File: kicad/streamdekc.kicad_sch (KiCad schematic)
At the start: 26 parts, among them IC1 74HC4051P, IC2 74HC4051P, SW1 SW_DIP_x01, SW2 SW_DIP_x01, SW3 SW_DIP_x01, SW4 SW_DIP_x01, SW5 SW_DIP_x01, SW6 SW_DIP_x01, SW7 SW_DIP_x01, SW8 SW_DIP_x01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

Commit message: Initial pcb design
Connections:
- net SW1: now also SW1.1
- net SW2: now also SW2.1
- net SW3: now also SW3.1
- net SW4: now also SW4.1
- net SW5: now also SW5.1
- net SW6: now also SW6.1
- net SW7: now also SW7.1
- net SW8: now also SW8.1
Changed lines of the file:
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@@
+    (stroke (width 0) (type default) (color 0 0 0 0))
+  )
+  (wire (pts (xy 87.63 73.66) (xy 90.17 73.66))
     (stroke (width 0) (type default) (color 0 0 0 0))
   )
@@
     (stroke (width 0) (type default) (color 0 0 0 0))
   )
+  (wire (pts (xy 87.63 62.23) (xy 90.17 62.23))
+    (stroke (width 0) (type default) (color 0 0 0 0))
+  )
   (wire (pts (xy 29.21 95.25) (xy 34.29 95.25))
     (stroke (width 0) (type default) (color 0 0 0 0))
@@
     (stroke (width 0) (type default) (color 0 0 0 0))
   )
+  (wire (pts (xy 114.3 73.66) (xy 116.84 73.66))
+    (stroke (width 0) (type default) (color 0 0 0 0))
+  )
   (wire (pts (xy 80.01 128.27) (xy 87.63 128.27))
     (stroke (width 0) (type default) (color 0 0 0 0))
@@
     (stroke (width 0) (type default) (color 0 0 0 0))
   )
+  (wire (pts (xy 87.63 96.52) (xy 90.17 96.52))
+    (stroke (width 0) (type default) (color 0 0 0 0))
+  )
   (wire (pts (xy 80.01 115.57) (xy 87.63 115.57))
     (stroke (width 0) (type default) (color 0 0 0 0))
@@
     (stroke (width 0) (type default) (color 0 0 0 0))
   )
+  (wire (pts (xy 114.3 62.23) (xy 116.84 62.23))
+    (stroke (width 0) (type default) (color 0 0 0 0))
+  )
   (wire (pts (xy 95.25 35.56) (xy 95.25 30.48))
     (stroke (width 0) (type default) (color 0 0 0 0))
@@
     (stroke (width 0) (type default) (color 0 0 0 0))
   )
+  (wire (pts (xy 87.63 85.09) (xy 90.17 85.09))
+    (stroke (width 0) (type default) (color 0 0 0 0))
+  )
   (wire (pts (xy 179.07 95.25) (xy 179.07 100.33))
     (stroke (width 0) (type default) (color 0 0 0 0))
@@
     (stroke (width 0) (type default) (color 0 0 0 0))
   )
+  (wire (pts (xy 114.3 85.09) (xy 116.84 85.09))
+    (stroke (width 0) (type default) (color 0 0 0 0))
+  )
   (wire (pts (xy 180.34 36.83) (xy 184.15 36.83))
     (stroke (width 0) (type default) (color 0 0 0 0))
@@
     (stroke (width 0) (type default) (color 0 0 0 0))
   )
+  (wire (pts (xy 114.3 96.52) (xy 116.84 96.52))
+    (stroke (width 0) (type default) (color 0 0 0 0))
+  )
   (wire (pts (xy 41.91 120.65) (xy 49.53 120.65))
     (stroke (width 0) (type default) (color 0 0 0 0))
@@
     (effects (font (size 1.27 1.27)) (justify left bottom))
   )
+  (label "SW2" (at 87.63 73.66 0)
+    (effects (font (size 1.27 1.27)) (justify left bottom))
+  )
   (label "D9" (at 49.53 39.37 0)
     (effects (font (size 1.27 1.27)) (justify left bottom))
   )
+  (label "SW1" (at 87.63 62.23 0)
+    (effects (font (size 1.27 1.27)) (justify left bottom))
+  )
   (label "3V3" (at 46.99 82.55 0)
     (effects (font (size 1.27 1.27)) (justify left bottom))
@@
     (effects (font (size 1.27 1.27)) (justify left bottom))
   )
+  (label "SW8" (at 114.3 96.52 0)
+    (effects (font (size 1.27 1.27)) (justify left bottom))
+  )
   (label "SDA_5V" (at 80.01 118.11 0)
     (effects (font (size 1.27 1.27)) (justify left bottom))
@@
     (effects (font (size 1.27 1.27)) (justify left bottom))
   )
+  (label "SW4" (at 87.63 96.52 0)
+    (effects (font (size 1.27 1.27)) (justify left bottom))
+  )
+  (label "SW6" (at 114.3 73.66 0)
+    (effects (font (size 1.27 1.27)) (justify left bottom))
+  )
   (label "SCL_5V" (at 184.15 77.47 0)
     (effects (font (size 1.27 1.27)) (justify left bottom))
@@
     (effects (font (size 1.27 1.27)) (justify left bottom))
   )
+  (label "SW7" (at 114.3 85.09 0)
+    (effects (font (size 1.27 1.27)) (justify left bottom))
+  )
   (label "SCL_5V" (at 160.02 97.79 0)
     (effects (font (size 1.27 1.27)) (justify left bottom))
@@
     (effects (font (size 1.27 1.27)) (justify left bottom))
   )
+  (label "SW5" (at 114.3 62.23 0)
+    (effects (font (size 1.27 1.27)) (justify left bottom))
+  )
   (label "DISP_5_SDA" (at 24.13 55.88 0)
     (effects (font (size 1.27 1.27)) (justify left bottom))
@@
     (effects (font (size 1.27 1.27)) (justify left bottom))
   )
+  (label "SW3" (at 87.63 85.09 0)
+    (effects (font (size 1.27 1.27)) (justify left bottom))
+  )

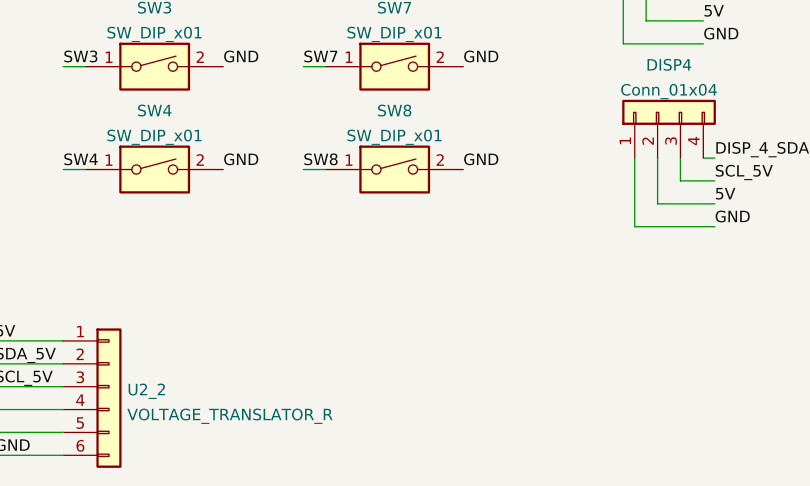
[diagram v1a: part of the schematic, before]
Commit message: Update assembly instructions on B.Silkscreen
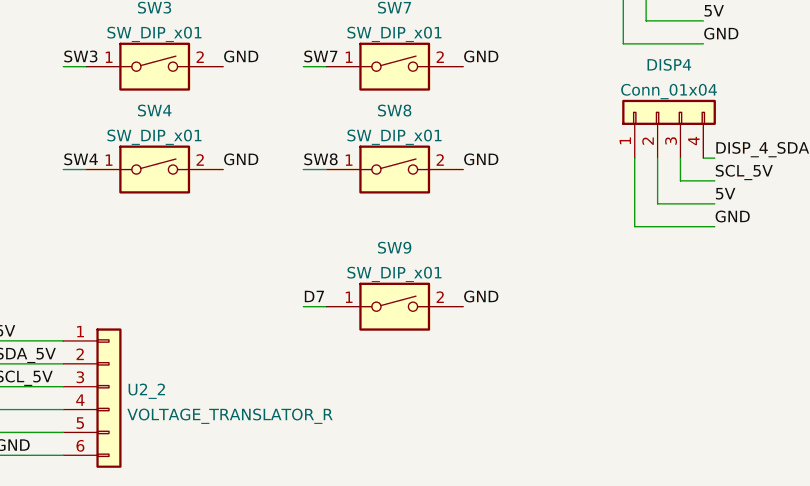
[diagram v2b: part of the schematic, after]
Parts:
- added SW9: SW_DIP_x01, Connector_PinHeader_2.54mm:PinHeader_1x02_P2.54mm_Vertical, symbol Switch:SW_DIP_x01
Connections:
- net D7: now also SW9.1
- net GND: now also SW9.2
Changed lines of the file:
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@@
+    (stroke (width 0) (type default) (color 0 0 0 0))
+  )
+  (wire (pts (xy 114.3 111.76) (xy 116.84 111.76))
     (stroke (width 0) (type default) (color 0 0 0 0))
   )
@@
     (effects (font (size 1.27 1.27)) (justify left bottom))
   )
+  (label "GND" (at 132.08 111.76 0)
+    (effects (font (size 1.27 1.27)) (justify left bottom))
+  )
   (label "5V" (at 158.75 59.69 0)
     (effects (font (size 1.27 1.27)) (justify left bottom))
@@
   )
   (label "5V" (at 184.15 80.01 0)
+    (effects (font (size 1.27 1.27)) (justify left bottom))
+  )
+  (label "D7" (at 114.3 111.76 0)
     (effects (font (size 1.27 1.27)) (justify left bottom))
   )
@@
     (pin "4")
   )
+  (symbol (lib_id "Switch:SW_DIP_x01") (at 124.46 111.76 0) (unit 1)
+    (in_bom yes) (on_board yes) (fields_autoplaced)
+    (property "Reference" "SW9" (id 0) (at 124.46 105.2535 0))
+    (property "Value" "SW_DIP_x01" (id 1) (at 124.46 108.0286 0))
+    (property "Footprint" "Connector_PinHeader_2.54mm:PinHeader_1x02_P2.54mm_Vertical" (id 2) (at 124.46 111.76 0)
+      (effects (font (size 1.27 1.27)) hide)
+    )
+    (property "Datasheet" "~" (id 3) (at 124.46 111.76 0)
+      (effects (font (size 1.27 1.27)) hide)
+    )
+    (pin "1")
+    (pin "2")
+  )
   (symbol (lib_id "Connector_Generic:Conn_01x06") (at 54.61 120.65 0) (unit 1)
     (in_bom yes) (on_board yes) (fields_autoplaced)
@@
       (reference "SW8") (unit 1) (value "SW_DIP_x01") (footprint "Library:Switch_2pin_6mm_p4.5mm")
     )
+    (path "/e5706f46-05e5-4013-b9f6-3b0eacd7b31e"
+      (reference "SW9") (unit 1) (value "SW_DIP_x01") (footprint "Connector_PinHeader_2.54mm:PinHeader_1x02_P2.54mm_Vertical")
+    )
     (path "/02ab6f40-3a6e-40e6-9c54-1e5e2097aa06"
